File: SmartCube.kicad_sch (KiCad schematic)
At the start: 81 parts, among them J1 TYPE-C, J2 XH, Q1 AO3401A, Q2 AO3401A, Q3 BC857, Q4 SS8050, Q5 SS8050, Q6 AO3400A, Q7 AO3400A, SW1 SW_Push, U1 AMS1117-3.3, U2 CP2102, U3 SHTC3, U4 MPU-6050, U5 INA226

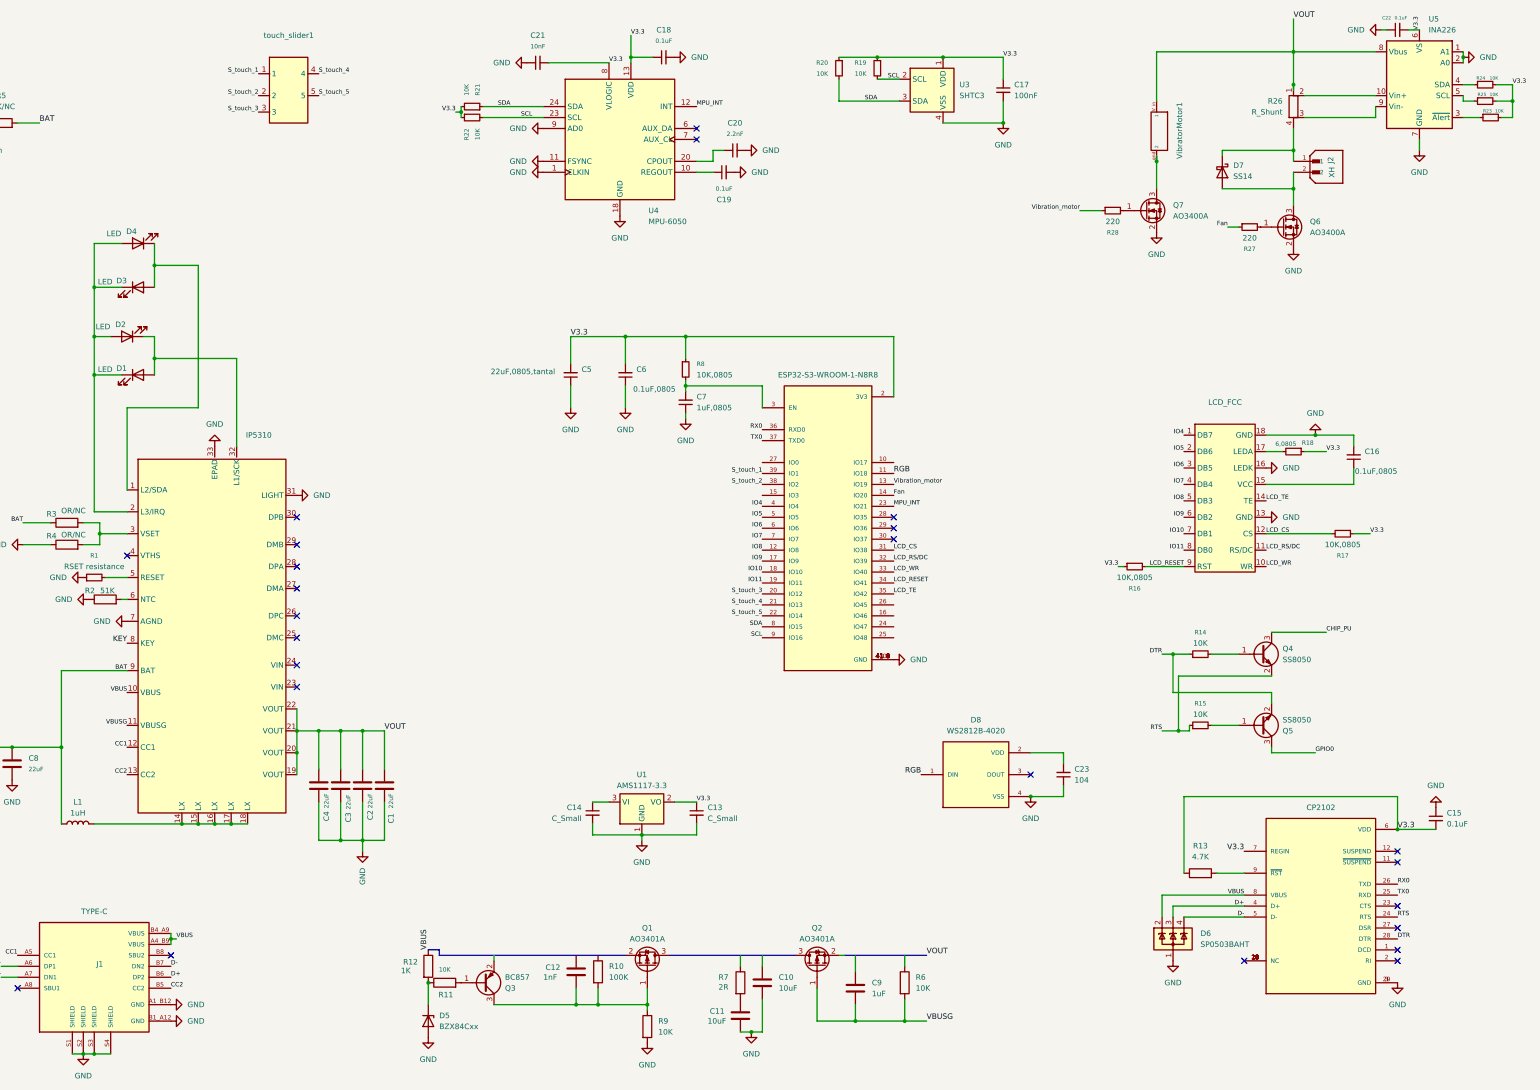
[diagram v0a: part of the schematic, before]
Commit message: Update Schema and add SP0502BAHAT
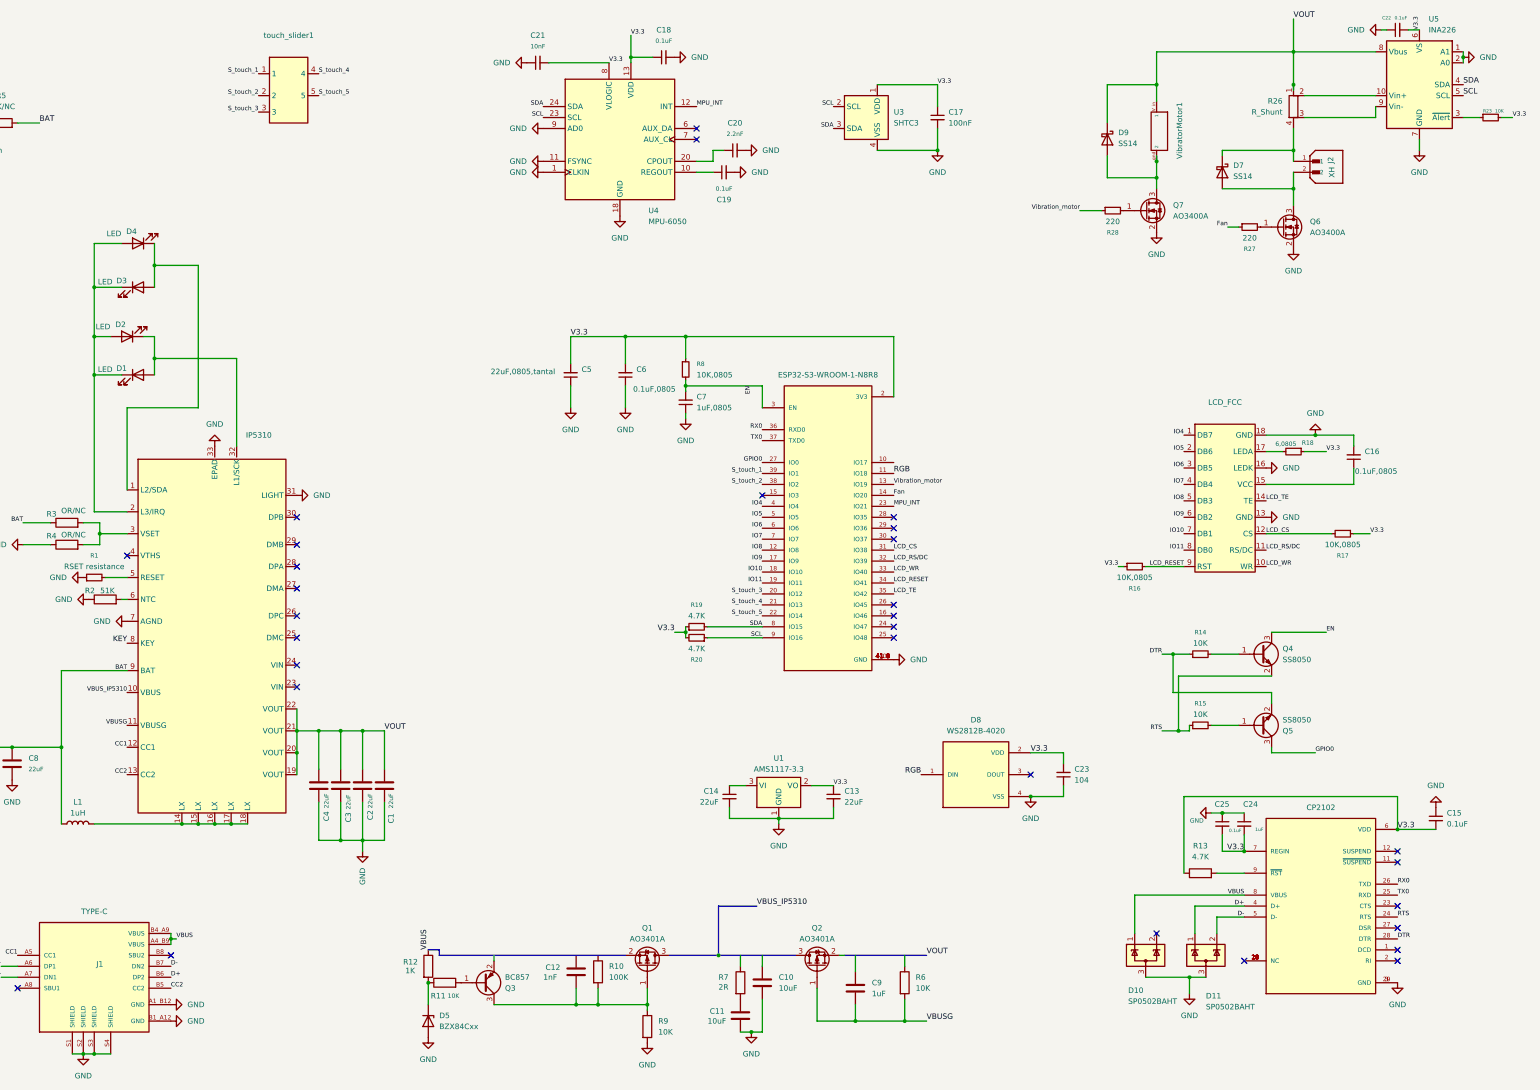
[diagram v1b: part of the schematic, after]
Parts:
- removed D6: SP0503BAHT, Package_TO_SOT_SMD:SOT-143, symbol Power_Protection:SP0503BAHT
- removed R21, R22, R24, R25: 10K, symbol Device:R_Small
- added C24: 1uF, symbol Device:C_Small
- added C25: 0.1uF, symbol Device:C_Small
- added D10, D11: SP0502BAHT, Package_TO_SOT_SMD:SOT-23, symbol Power_Protection:SP0502BAHT
- added D9: SS14, Diode_SMD:D_SMA, symbol Diode:SS14
- C13, C14: value C_Small -> 22uF
- R19, R20: value 10K -> 4.7K
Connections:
- net CHIP_PU is gone; now on net EN: Q4.3 (C)
- net D+: now also D11.1 (K)
- net D-: now also D11.2 (K)
- net GND: now also C24.1, C25.1, D10.3 (A), D11.3 (A)
- net GPIO0: now also ESP32-S3-WROOM-1-N8R8.27 (IO0)
- net SCL: now also R20.1, U5.5 (SCL); no longer R19.2
- net SDA: now also R19.2, U5.4 (SDA); no longer R20.2
- net V3.3: now also C23.2, D8.2 (VDD), R20.2, C24.2, C25.2; no longer R20.1
- net VBUS: now also D10.1 (K); no longer IP5310.10 (VBUS)
- net VOUT: now also D9.1 (K)
- net at Q7.3 (D), VibratorMotor1.gnd (2): now also D9.2 (A)
- net EN: now reaches C7.2, ESP32-S3-WROOM-1-N8R8.3 (EN), R8.2
- new net VBUS_IP5310: IP5310.10 (VBUS)
- no-connect marks 24 -> 30
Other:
- moved on the sheet: C13, C14, C17, U1, U3

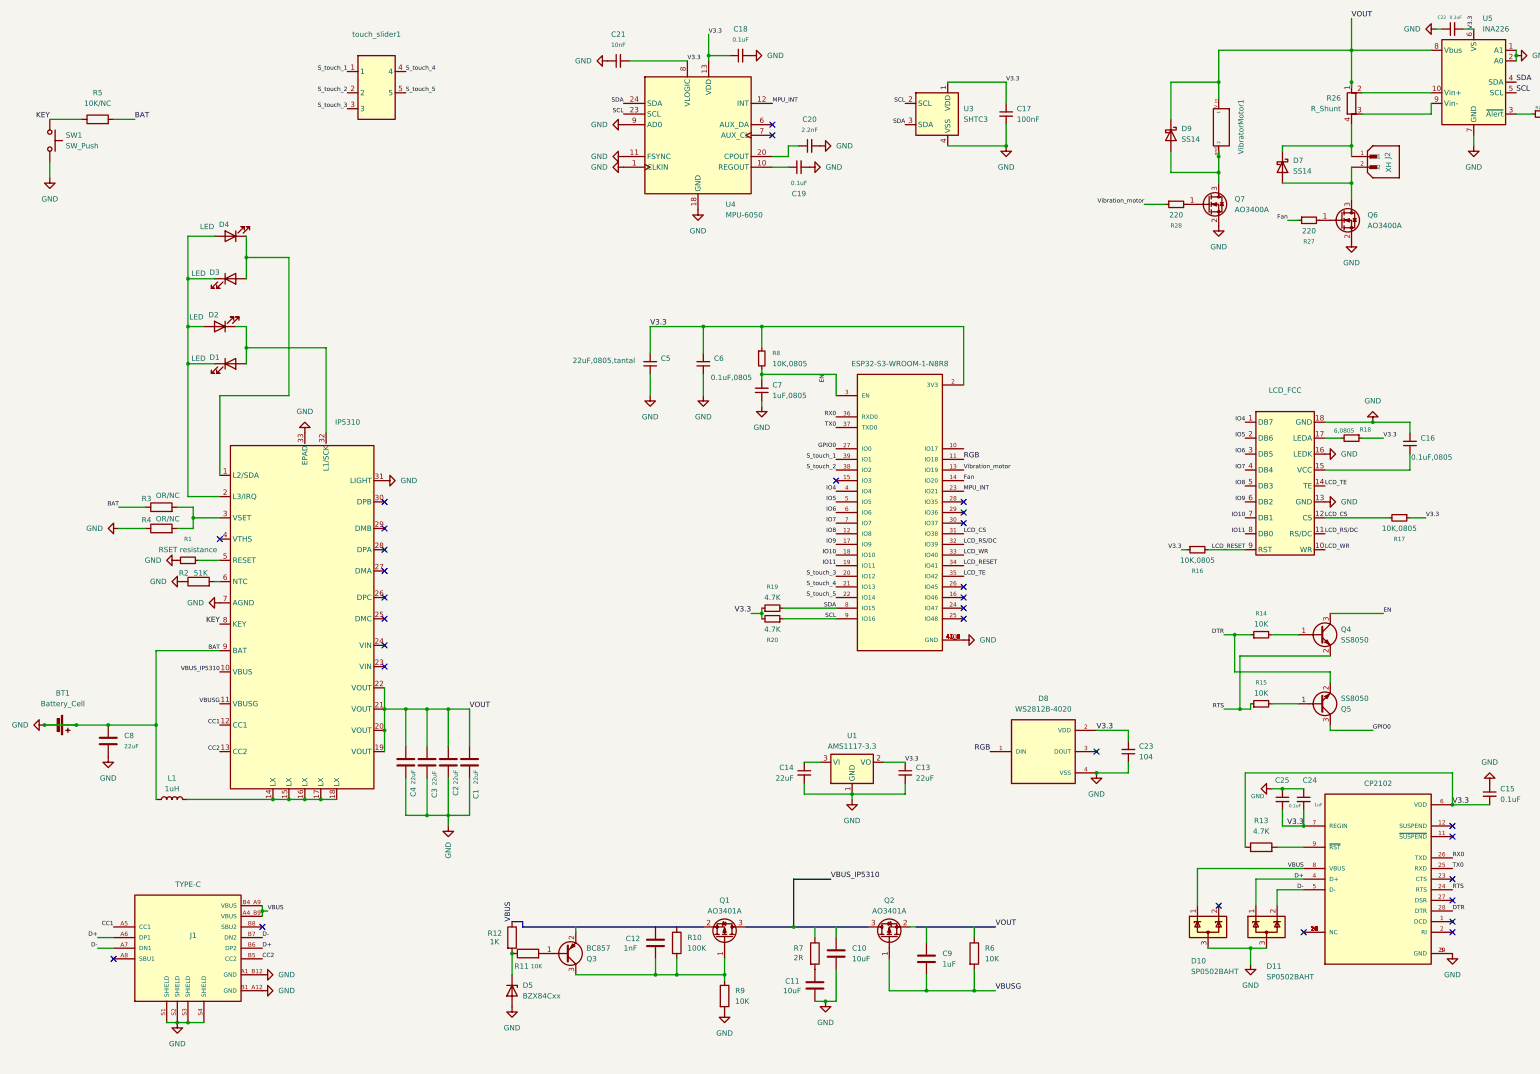
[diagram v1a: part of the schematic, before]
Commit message: Add footprints to schema
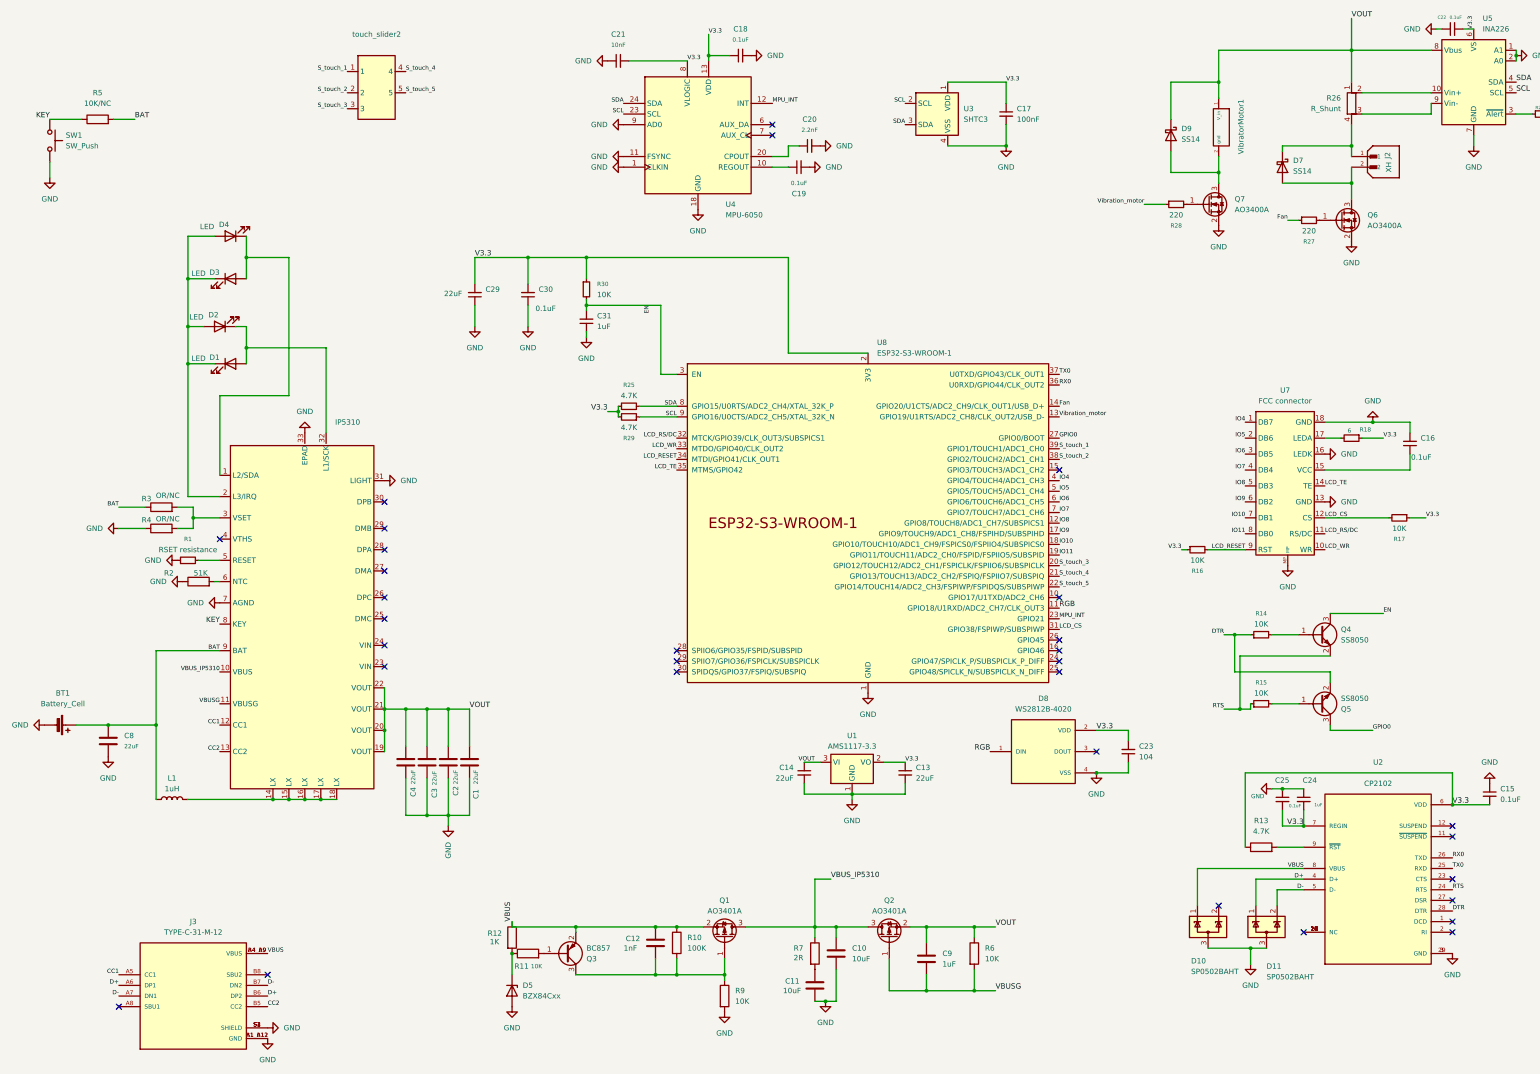
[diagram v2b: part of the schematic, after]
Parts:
- removed C5: 22uF,0805,tantal, symbol Device:C_Small
- removed C6: 0.1uF,0805, symbol Device:C_Small
- removed C7: 1uF,0805, symbol Device:C_Small
- removed ESP32-S3-WROOM-1-N8R8: ESP32-S3-WROOM-1-N8R8, ESP32-S3-WROOM-1-N8R8:XCVR_ESP32S3WROOM1N8R8, symbol ESP32-S3-WROOM-1-N8R8:ESP32-S3-WROOM-1-N8R8
- removed J1: TYPE-C, TYPE-C-31-M-12:HRO_TYPE-C-31-M-12, symbol TYPE-C-31-M-12:TYPE-C-31-M-12
- removed LCD_FCC: ~, connector:FPC_18, symbol fpc18:fpc18
- removed R19, R20: 4.7K, symbol Device:R_Small
- removed R8: 10K,0805, symbol Device:R_Small
- removed touch_slider1: ~, 5pin-touch-slider:TouchSlider-5_50x10mm, symbol 5pin-touch-slider:5pin_touch_slider_
- added C29: 22uF, Capacitor_Tantalum_SMD:CP_EIA-3528-21_Kemet-B, symbol Device:C_Small
- added C30: 0.1uF, Capacitor_SMD:C_0805_2012Metric, symbol Device:C_Small
- added C31: 1uF, Capacitor_SMD:C_0805_2012Metric, symbol Device:C_Small
- added J3: TYPE-C-31-M-12, TYPE-C-31-M-12:HRO_TYPE-C-31-M-12, symbol TYPE-C-31-M-12:TYPE-C-31-M-12
- added R25, R29: 4.7K, Resistor_SMD:R_0805_2012Metric, symbol Device:R_Small
- added R30: 10K, Resistor_SMD:R_0805_2012Metric, symbol Device:R_Small
- added U7: FCC connector, FCC 18 pin 0.5:FPC_18 0.5, symbol fpc18:fpc18
- added U8: ESP32-S3-WROOM-1, PCM_Espressif:ESP32-S3-WROOM-1, symbol PCM_Espressif:ESP32-S3-WROOM-1
- added touch_slider2: ~, Touch Slider:TouchSlider-5_50x10mm, symbol 5pin-touch-slider:5pin_touch_slider_
- BT1: footprint (none) -> Vibrator Motor:vibrator connector
- C1, C10, C11, C12, C13, C14, C15, C17, C18, C19, C2, C20, C21, C22, C23, C24, C25, C3, C4, C8, C9: footprint (none) -> Capacitor_SMD:C_0805_2012Metric
- C16: value 0.1uF,0805 -> 0.1uF; footprint (none) -> Capacitor_SMD:C_0805_2012Metric
- D1, D2, D3, D4: footprint (none) -> LED_SMD:LED_0603_1608Metric
- IP5310: footprint ip5310:QFN-32_EP_5x5_Pitch0.5mm -> IP5310:IP5310
- L1: footprint (none) -> Inductor_SMD:L_7.3x7.3_H4.5
- R1, R10, R11, R12, R13, R14, R15, R23, R27, R28, R3, R4, R5, R6, R7, R9: footprint (none) -> Resistor_SMD:R_0805_2012Metric
- R16, R17: value 10K,0805 -> 10K; footprint (none) -> Resistor_SMD:R_0805_2012Metric
- R18: value 6,0805 -> 6; footprint (none) -> Resistor_SMD:R_0805_2012Metric
- R2: footprint (none) -> Resistor_SMD:R_0603_1608Metric
- R26: footprint (none) -> Resistor_SMD:R_Shunt_Vishay_WSK2512_6332Metric_T1.19mm
- SW1: footprint (none) -> Button_Switch_SMD:SW_SPST_EVQP2_MiddlePushTravel_H2.5mm
- VibratorMotor1: footprint Vibrator Motor:ConnectorMicromatch-2 -> Vibrator Motor:vibrator connector
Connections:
- net CC1: now also J3.A5 (CC1)
- net CC2: now also J3.B5 (CC2)
- net D+: now also J3.A6 (DP1), J3.B6 (DP2)
- net D-: now also J3.A7 (DN1), J3.B7 (DN2)
- net EN: now also C31.2, R30.2, U8.3 (EN)
- net Fan: now also U8.14 (GPIO20/U1CTS/ADC2_CH9/CLK_OUT1/USB_D+)
- net GND: now also C29.1, C30.1, C31.1, J3.A1_B12 (GND), J3.B1_A12 (GND), J3.S1 (SHIELD), J3.S2 (SHIELD), J3.S3 (SHIELD), J3.S4 (SHIELD), U7.13 (GND), U7.16 (LEDK), U7.18 (GND), U7.MP, U8.1 (GND), U8.40 (GND), U8.41 (GND); no longer BT1.1 (+), C8.1, IP5310.9 (BAT), L1.1, R3.1, R5.2
- net GPIO0: now also U8.27 (GPIO0/BOOT)
- net IO10: now also U7.7 (DB1), U8.18 (GPIO10/TOUCH10/ADC1_CH9/FSPICS0/FSPIIO4/SUBSPICS0)
- net IO11: now also U7.8 (DB0), U8.19 (GPIO11/TOUCH11/ADC2_CH0/FSPID/FSPIIO5/SUBSPID)
- net IO4: now also U7.1 (DB7), U8.4 (GPIO4/TOUCH4/ADC1_CH3)
- net IO5: now also U7.2 (DB6), U8.5 (GPIO5/TOUCH5/ADC1_CH4)
- net IO6: now also U7.3 (DB5), U8.6 (GPIO6/TOUCH6/ADC1_CH5)
- net IO7: now also U7.4 (DB4), U8.7 (GPIO7/TOUCH7/ADC1_CH6)
- net IO8: now also U7.5 (DB3), U8.12 (GPIO8/TOUCH8/ADC1_CH7/SUBSPICS1)
- net IO9: now also U7.6 (DB2), U8.17 (GPIO9/TOUCH9/ADC1_CH8/FSPIHD/SUBSPIHD)
- net LCD_CS: now also U7.12 (CS), U8.31 (GPIO38/FSPIWP/SUBSPIWP)
- net LCD_RESET: now also U7.9 (RST), U8.34 (MTDI/GPIO41/CLK_OUT1)
- net LCD_RS/DC: now also U7.11 (RS/DC), U8.32 (MTCK/GPIO39/CLK_OUT3/SUBSPICS1)
- net LCD_TE: now also U7.14 (TE), U8.35 (MTMS/GPIO42)
- net LCD_WR: now also U7.10 (WR), U8.33 (MTDO/GPIO40/CLK_OUT2)
- net MPU_INT: now also U8.23 (GPIO21)
- net RGB: now also U8.11 (GPIO18/U1RXD/ADC2_CH7/CLK_OUT3)
- net RX0: now also U8.36 (U0RXD/GPIO44/CLK_OUT2)
- net SCL: now also R29.1, U8.9 (GPIO16/U0CTS/ADC2_CH5/XTAL_32K_N)
- net SDA: now also R25.2, U8.8 (GPIO15/U0RTS/ADC2_CH4/XTAL_32K_P)
- net S_touch_1: now also U8.39 (GPIO1/TOUCH1/ADC1_CH0), touch_slider2.1
- net S_touch_2: now also U8.38 (GPIO2/TOUCH2/ADC1_CH1), touch_slider2.2
- net S_touch_3: now also U8.20 (GPIO12/TOUCH12/ADC2_CH1/FSPICLK/FSPIIO6/SUBSPICLK), touch_slider2.3
- net S_touch_4: now also U8.21 (GPIO13/TOUCH13/ADC2_CH2/FSPIQ/FSPIIO7/SUBSPIQ), touch_slider2.4
- net S_touch_5: now also U8.22 (GPIO14/TOUCH14/ADC2_CH3/FSPIWP/FSPIDQS/SUBSPIWP), touch_slider2.5
- net TX0: now also U8.37 (U0TXD/GPIO43/CLK_OUT1)
- net V3.3: now also C29.2, C30.2, R25.1, R29.2, R30.1, U8.2 (3V3)
- net VBUS: now also C12.1, Q1.2 (S), Q3.2 (E), R10.1, J3.A4_B9 (VBUS), J3.B4_A9 (VBUS)
- net VBUS_IP5310: now also C10.1, Q1.3 (D), Q2.3 (D), R7.1
- net VOUT: now also C14.1, C9.1, Q2.2 (S), R6.1, U1.3 (VI), VibratorMotor1.1 (V_in); no longer VibratorMotor1.V_in (1)
- net Vibration_motor: now also U8.13 (GPIO19/U1RTS/ADC2_CH8/CLK_OUT2/USB_D-)
- net at D9.2 (A), Q7.3 (D): now also VibratorMotor1.2 (gnd); no longer VibratorMotor1.gnd (2)
- net at C16.1: now also U7.15 (VCC)
- net at R18.2: now also U7.17 (LEDA)
- new net BAT: BT1.1 (+), C8.1, IP5310.9 (BAT), L1.1, R3.1, R5.2
- no-connect marks 30 -> 31

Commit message: Add first version of pcb
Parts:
- removed J3: TYPE-C-31-M-12, TYPE-C-31-M-12:HRO_TYPE-C-31-M-12, symbol TYPE-C-31-M-12:TYPE-C-31-M-12
- removed U2: CP2102, CP2102:QFN50P500X500X100-29N, symbol CP2102:CP2102
- added J1: USB_C_Receptacle_USB2.0_16P, Connector_USB:USB_C_Receptacle_GCT_USB4105-xx-A_16P_TopMnt_Horizontal, symbol Connector:USB_C_Receptacle_USB2.0_16P
- added U6: CP2102, CP2102:QFN50P500X500X100-29N, symbol CP2102:CP2102
- J2: footprint B2B-XH-A__LF__SN_:JST_B2B-XH-A__LF__SN_ -> Vibrator Motor:vibrator connector
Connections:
- net CC1: now also J1.A5 (CC1)
- net CC2: now also J1.B5 (CC2)
- net D+: now also J1.A6 (D+), J1.B6 (D+), U6.4 (D+)
- net D-: now also J1.A7 (D-), J1.B7 (D-), U6.5 (D-)
- net DTR: now also U6.28 (DTR)
- net GND: now also J1.A1 (GND), J1.A12 (GND), J1.B1 (GND), J1.B12 (GND), J1.S1 (SHIELD), U6.29 (GND), U6.3 (GND)
- net RTS: now also U6.24 (RTS)
- net RX0: now also U6.26 (TXD)
- net TX0: now also U6.25 (RXD)
- net V3.3: now also C16.1, U7.15 (VCC), U6.6 (VDD), U6.7 (REGIN)
- net VBUS: now also J1.A4 (VBUS), J1.A9 (VBUS), J1.B4 (VBUS), J1.B9 (VBUS), U6.8 (VBUS)
- net at R13.2: now also U6.9 (~{RST})
- new net: U6.10 (NC), U6.13 (NC), U6.14 (NC), U6.15 (NC), U6.16 (NC), U6.17 (NC), U6.18 (NC), U6.19 (NC), U6.20 (NC), U6.21 (NC), U6.22 (NC)
